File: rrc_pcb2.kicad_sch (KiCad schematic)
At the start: 19 parts, among them J1 battery_header, J2 buzzer_toggle_pin, U1 INA260, U2 Teensy4.1, U3 BN220-GPS, U5 MS5611, U6 logo, U7 voltReg

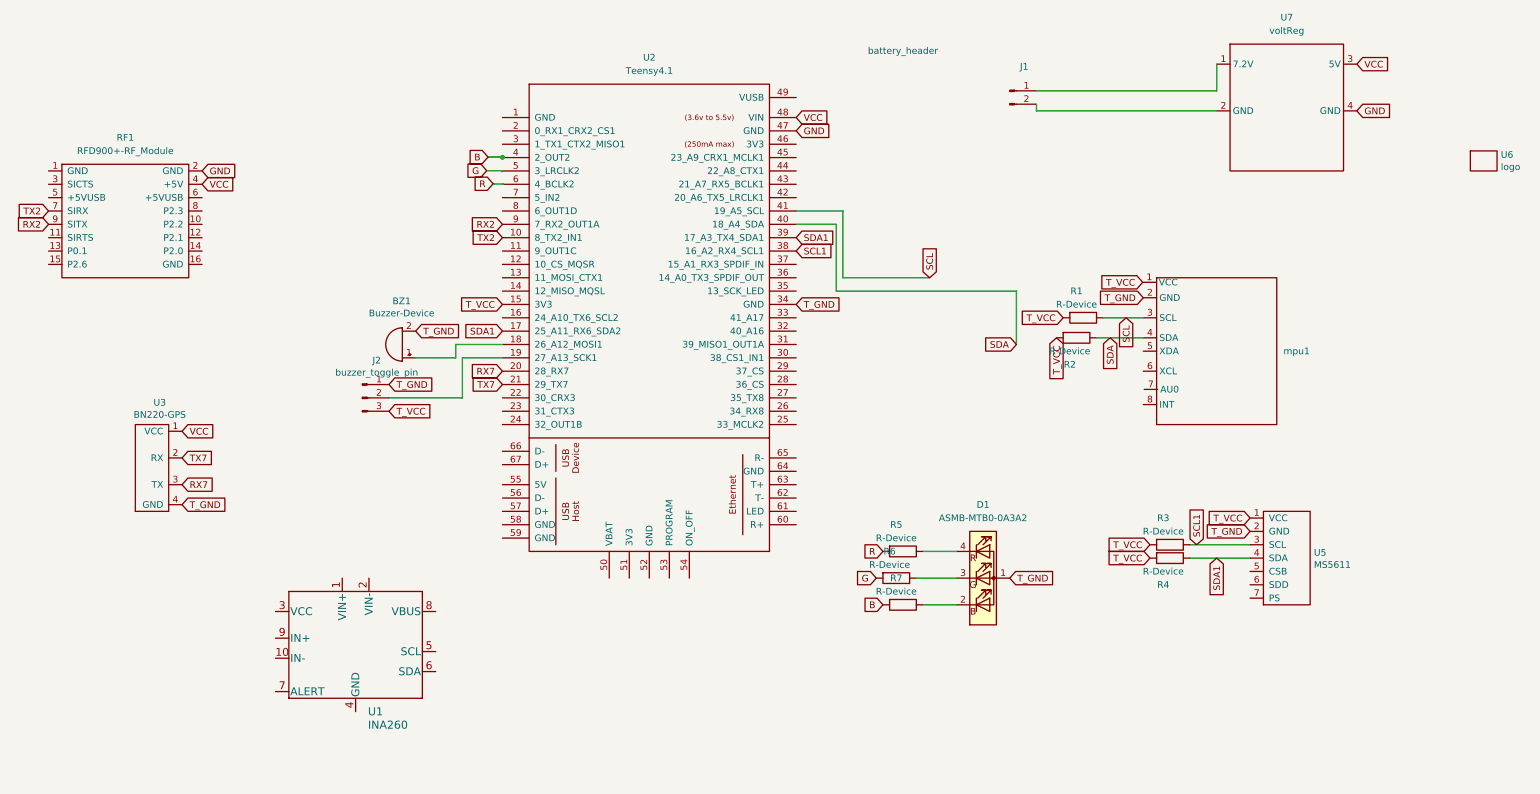
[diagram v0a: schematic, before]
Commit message: updated pcb ina160 and traces
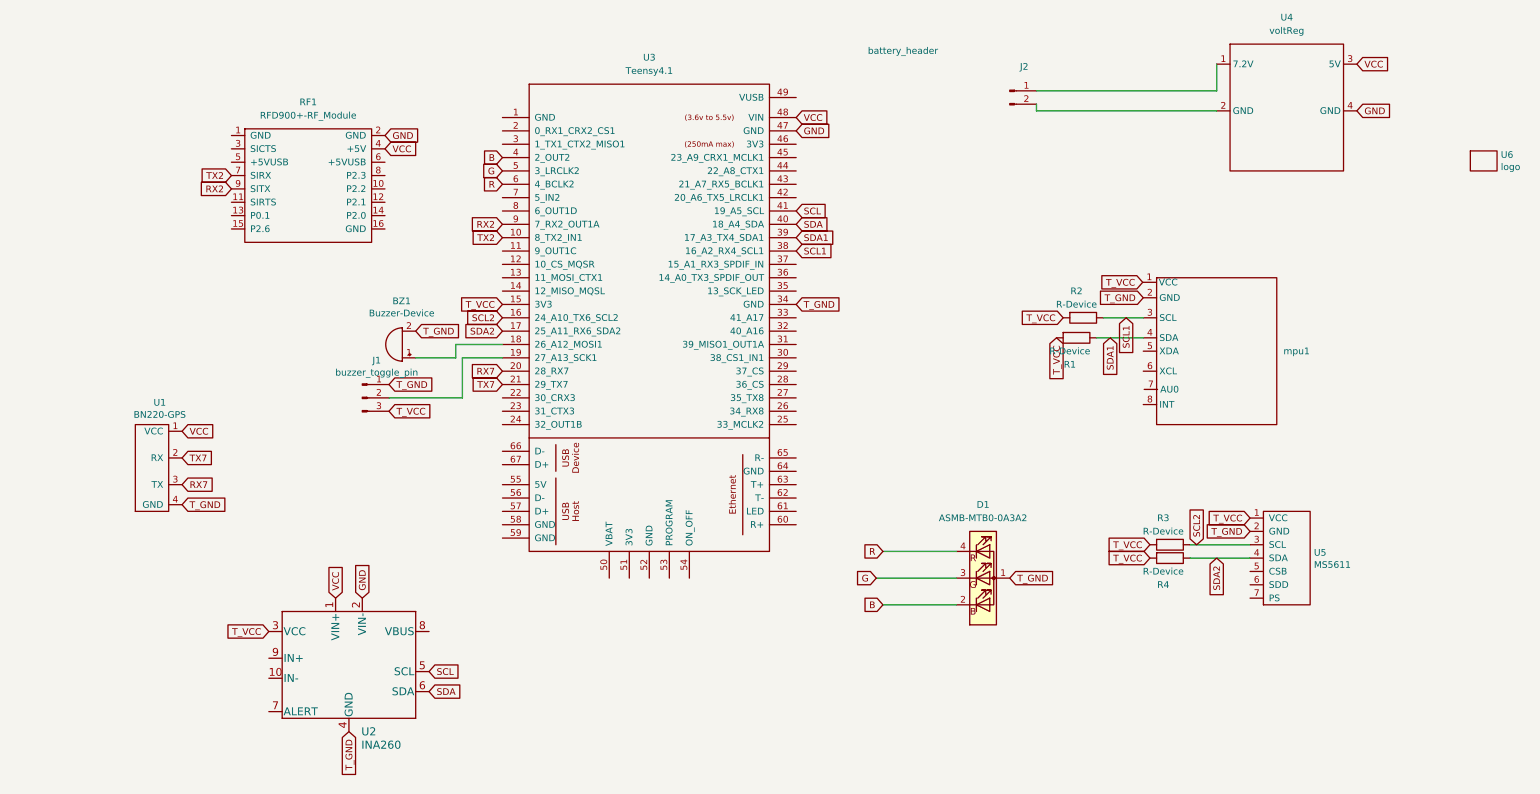
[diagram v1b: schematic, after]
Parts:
- removed R5, R6, R7: R-Device, Resistor_THT:R_Axial_DIN0207_L6.3mm_D2.5mm_P10.16mm_Horizontal, symbol rrc_pcb-rescue:R-Device
- removed U1: INA260, INA260:INA260, symbol parts:INA260
- added U2: INA260, INA260:INA260, symbol parts:INA260
- BZ1: footprint Buzzer_Beeper:Buzzer_12x9.5RM7.6 -> rfd900+:RFD900+
- renumbered J2 to J1, J1 to J2, R2 to R1, R1 to R2, U3 to U1, U2 to U3, U7 to U4
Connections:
- net B: now also D1.2 (BK), U3.4 (2_OUT2)
- net G: now also D1.3 (GK), U3.5 (3_LRCLK2)
- net GND: now also U2.2 (VIN-)
- net R: now also D1.4 (RK), U3.6 (4_BCLK2)
- net SCL: now also U2.5 (SCL); no longer R2.1, mpu1.3 (SCL)
- net SCL1: now also R2.1, mpu1.3 (SCL); no longer R3.1, U5.3 (SCL)
- net SDA: now also U2.6 (SDA); no longer R1.1, mpu1.4 (SDA)
- net SDA1: now also R1.1, mpu1.4 (SDA); no longer R4.1, U3.17 (25_A11_RX6_SDA2), U5.4 (SDA)
- net T_GND: now also U2.4 (GND)
- net T_VCC: now also U2.3 (VCC)
- net VCC: now also U2.1 (VIN+)
- net SCL2: now reaches U3.16 (24_A10_TX6_SCL2)
- net SCL2: now also R3.1, U5.3 (SCL)
- new net SDA2: R4.1, U3.17 (25_A11_RX6_SDA2), U5.4 (SDA)

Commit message: pcb gerber zip
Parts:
- BZ1: footprint rfd900+:RFD900+ -> Buzzer_Beeper:Buzzer_12x9.5RM7.6
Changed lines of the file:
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@@
       (effects (font (size 1.27 1.27)))
     )
-    (property "Footprint" "rfd900+:RFD900+" (at 80.645 67.31 90)
+    (property "Footprint" "Buzzer_Beeper:Buzzer_12x9.5RM7.6" (at 80.645 67.31 90)
       (effects (font (size 1.27 1.27)) hide)
     )
@@
       (effects (font (size 1.524 1.524)))
     )
-    (pin "8")
+    (pin "1")
+    (pin "10")
+    (pin "2")
+    (pin "3")
     (pin "4")
-    (pin "3")
-    (pin "9")
     (pin "5")
     (pin "6")
-    (pin "10")
     (pin "7")
-    (pin "2")
-    (pin "1")
+    (pin "8")
+    (pin "9")
     (instances
       (project "rrc_pcb2"

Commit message: updated rrc_pcb2 schematic and pcb files
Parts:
- removed D1: ASMB-MTB0-0A3A2, LED_4pin:LED_4PIN, symbol LED:ASMB-MTB0-0A3A2

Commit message: big cleanup of files
also new teensy4.1 symbo(the accurate one now) and fixed rfd900 schematic
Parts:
- U3: symbol teensy:Teensy4.1 -> parts:Teensy4.1
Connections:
- net B: now also U3.2 (2_OUT2); no longer U3.4 (2_OUT2)
- net G: now also U3.3 (3_LRCLK2); no longer U3.5 (3_LRCLK2)
- net GND: now also U3. (GND); no longer U3.47 (GND)
- net R: now also U3.4 (4_BCLK2); no longer U3.6 (4_BCLK2)
- net RX2: now also U3.7 (7_RX2_OUT1A); no longer U3.9 (7_RX2_OUT1A)
- net RX7: now also U3.28 (28_RX7); no longer U3.20 (28_RX7)
- net SCL: now also U3.19 (19_A5_SCL); no longer U3.41 (19_A5_SCL)
- net SCL1: now also U3.16 (16_A2_RX4_SCL1); no longer U3.38 (16_A2_RX4_SCL1)
- net SCL2: now also U3.24 (24_A10_TX6_SCL2); no longer U3.16 (24_A10_TX6_SCL2)
- net SDA: now also U3.18 (18_A4_SDA); no longer U3.40 (18_A4_SDA)
- net SDA1: now also U3.17 (17_A3_TX4_SDA1); no longer U3.39 (17_A3_TX4_SDA1)
- net SDA2: now also U3.25 (25_A11_RX6_SDA2); no longer U3.17 (25_A11_RX6_SDA2)
- net TX2: now also U3.8 (8_TX2_IN1); no longer U3.10 (8_TX2_IN1)
- net TX7: now also U3.29 (29_TX7); no longer U3.21 (29_TX7)
- net T_VCC: now also U3. (GND); no longer U3.15 (3V3)
- net VCC: now also RF1.5 (+5VUSB), U3. (GND); no longer RF1.4 (+5V), U3.48 (VIN)
- net at BZ1.1 (-): now also U3.26 (26_A12_MOSI1); no longer U3.18 (26_A12_MOSI1)
- net at J1.2 (Pin_2): now also U3.27 (27_A13_SCK1); no longer U3.19 (27_A13_SCK1)
- net at RF1.6 (+5VUSB): now also RF1.4 (+5V)

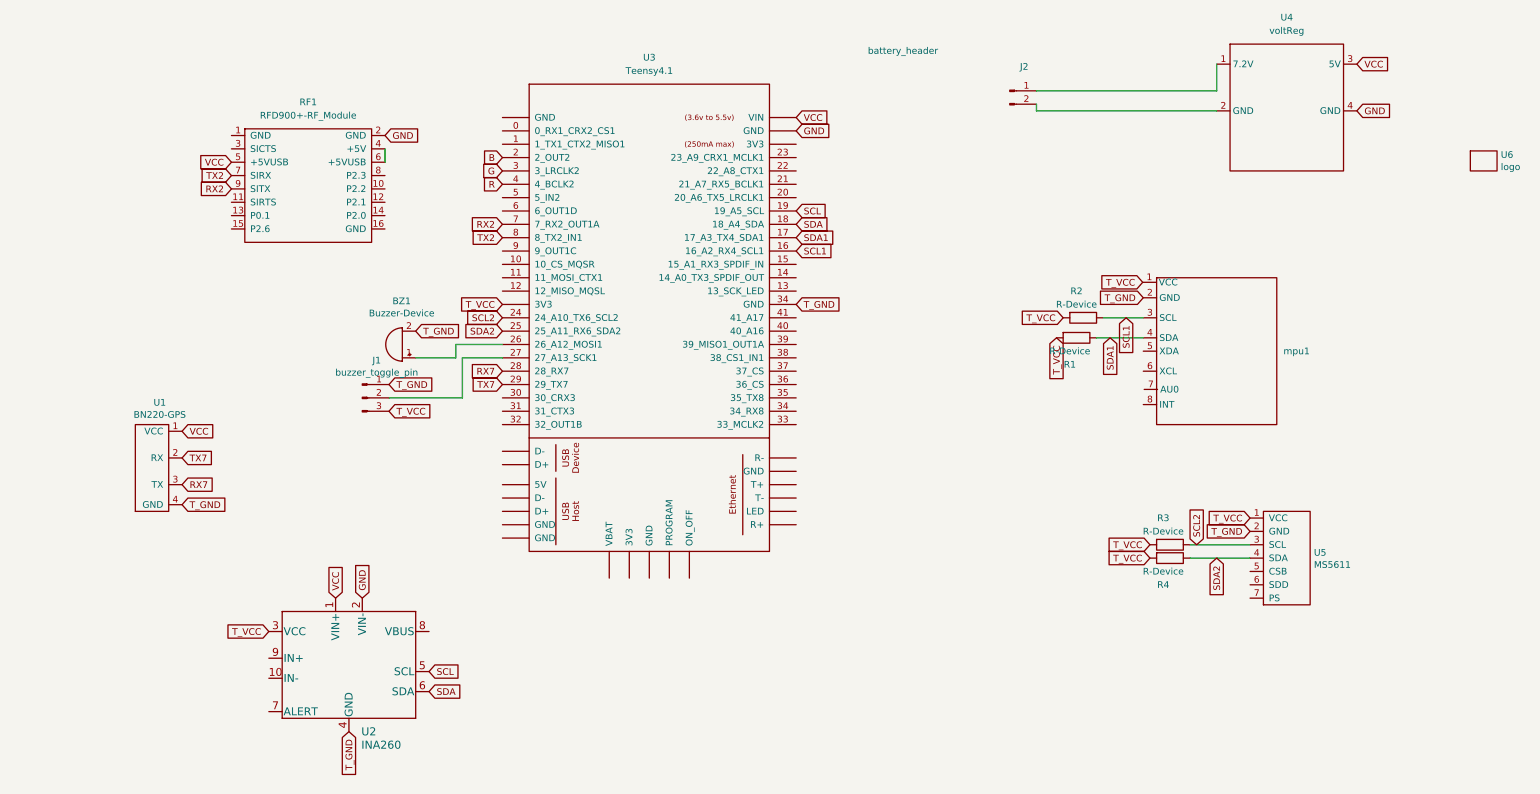
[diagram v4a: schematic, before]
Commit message: fixed rfd and netlists for teensy4.1
fixed the rfd netlists and teensy pwr netlists and also fixed the pinout and wiring for rfd
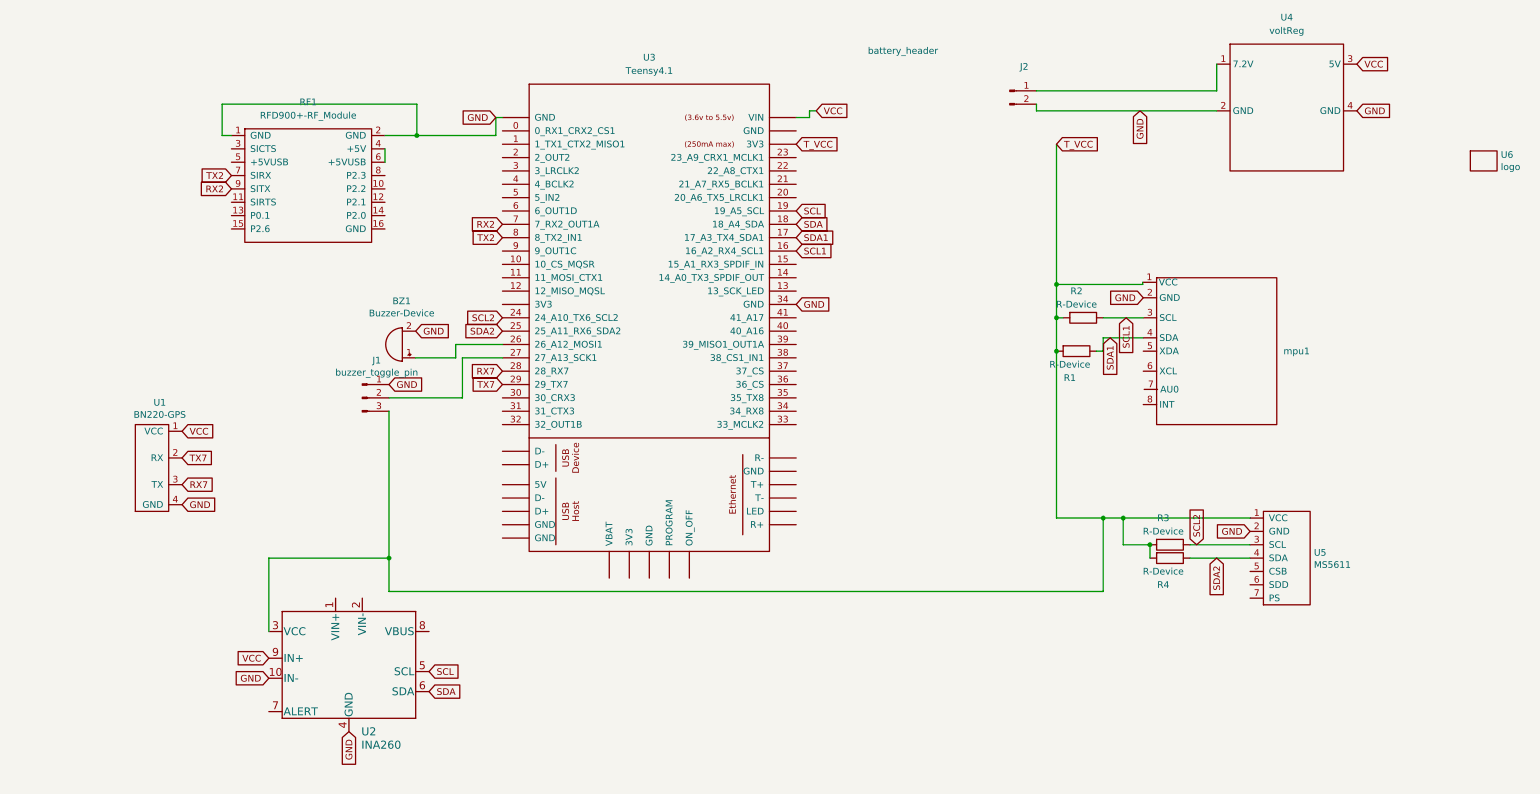
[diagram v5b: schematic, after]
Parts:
- J2: footprint Connector_JST:JST_GH_SM02B-GHS-TB_1x02-1MP_P1.25mm_Horizontal -> Connector_PinSocket_2.54mm:PinSocket_1x02_P2.54mm_Horizontal
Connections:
- net T_GND is gone; now on net GND: BZ1.2 (+), J1.1 (Pin_1), U1.4 (GND), U2.4 (GND), U3.34 (GND), U5.2 (GND), mpu1.2 (GND)
- net GND: now also J2.2 (Pin_2), RF1.1 (GND), U2.10 (IN-), U4.2 (GND); no longer U2.2 (VIN-)
- net VCC: now also U2.9 (IN+); no longer RF1.5 (+5VUSB), U2.1 (VIN+)
- net B: no longer names the net of U3.2 (2_OUT2)
- net G: no longer names the net of U3.3 (3_LRCLK2)
- net R: no longer names the net of U3.4 (4_BCLK2)
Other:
- moved on the sheet: R1
